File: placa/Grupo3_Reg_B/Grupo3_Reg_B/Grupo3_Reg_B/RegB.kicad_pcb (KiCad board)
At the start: 2 copper layers, 100 x 80 mm, 56 parts, among them J1 Conn_02x07_Counter_Clockwise_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, J2 OP295, J3 Conn_01x02_Pin, J4 Conn_01x02_Pin, J5 Conn_01x02_Pin, Q1 BC847BPN, Q10 BS170, Q3 2N2222, Q4 2N2222, Q5 BC547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

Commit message: modificacion de pcb
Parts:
- removed R29: 20, Resistor_THT:R_Axial_DIN0204_L3.6mm_D1.6mm_P7.62mm_Horizontal
- R26: value 2,4k -> 2,7k
- R27: value 1,1K -> 1,2K
- R5: value 3,3K -> 3,6K
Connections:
- R27 pad 1: Net-(R27-Pad1) -> GND
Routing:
- net Net-(R27-Pad1): track 5.47 -> 0.00 mm
- net Net-(Q1A-C1): track 61.7 -> 63.5 mm

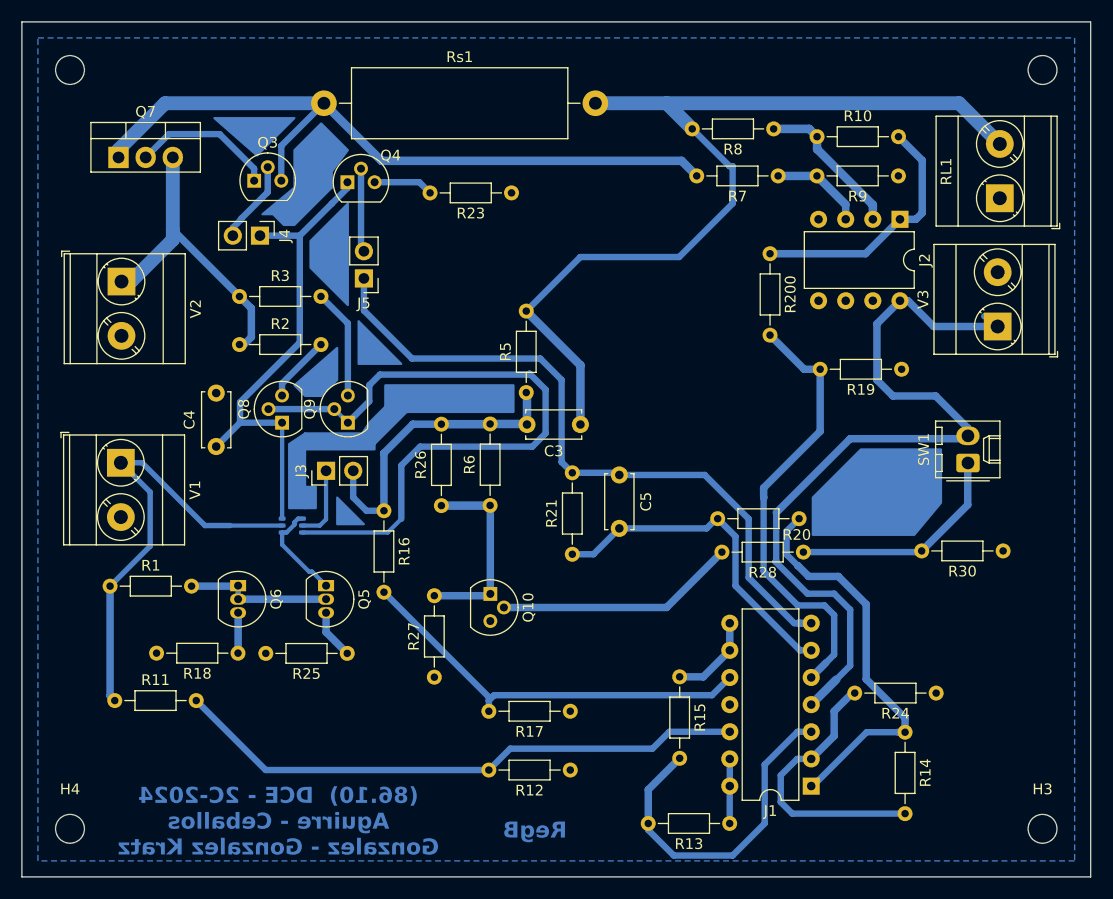
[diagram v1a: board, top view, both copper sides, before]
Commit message: caps de filtro de ruido de linea
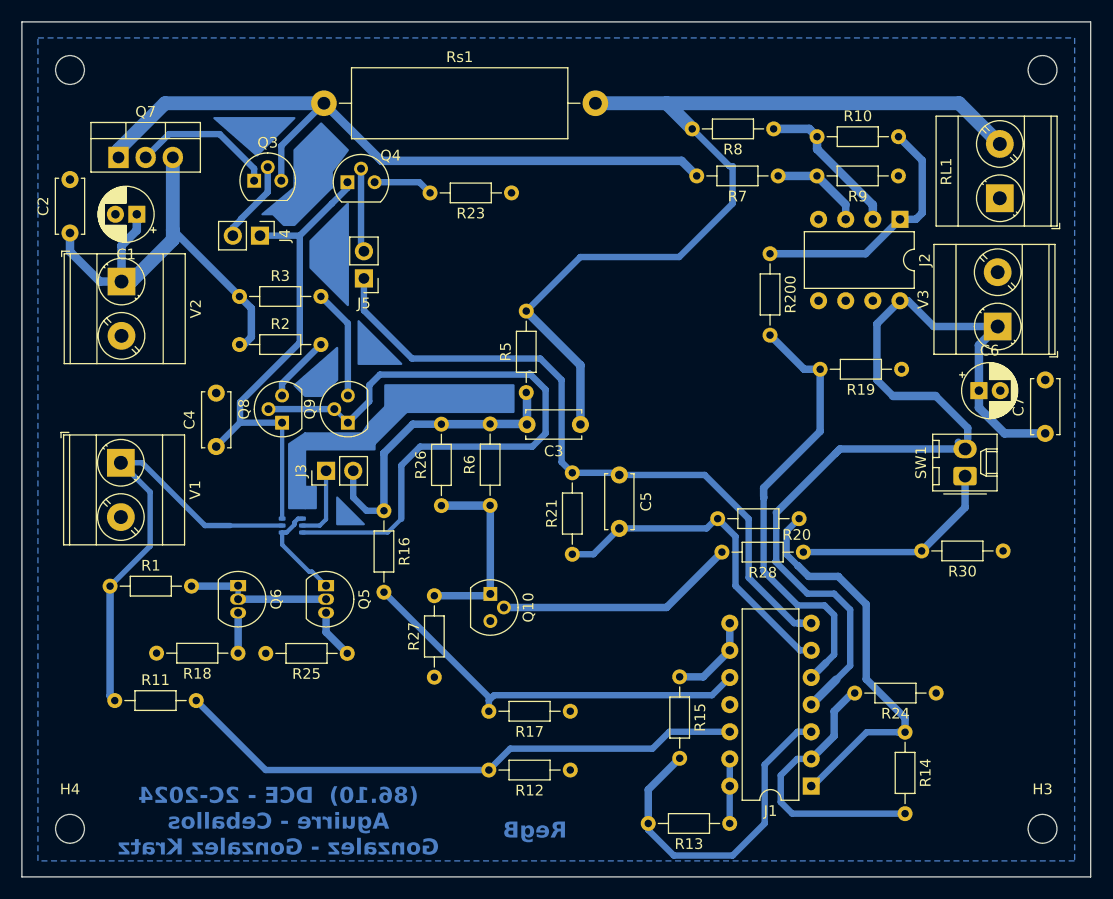
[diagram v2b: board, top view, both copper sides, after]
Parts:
- added C1: 10u, Capacitor_THT:CP_Radial_D5.0mm_P2.00mm, F.Cu at (88.8, 52.0)
- added C2: 10n, Capacitor_THT:C_Disc_D5.0mm_W2.5mm_P5.00mm, F.Cu at (82.5, 53.8)
- added C6: 10u, Capacitor_THT:CP_Radial_D5.0mm_P2.00mm, F.Cu at (167.5, 68.5)
- added C7: 10n, Capacitor_THT:C_Disc_D5.0mm_W2.5mm_P5.00mm, F.Cu at (173.8, 72.5)
- moved SW1 1.26 mm to (166.2, 76.5)
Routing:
- net Vreg: track 28.6 -> 43.2 mm
- net V_sup: track 75.7 -> 90.2 mm
- net Net-(R28-Pad1): track 21.4 -> 19.8 mm
